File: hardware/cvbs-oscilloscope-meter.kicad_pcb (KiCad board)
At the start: 2 copper layers, 49.5 x 99.7 mm, 40 parts, among them J1 Conn_Coaxial_Power, J2 Conn_Coaxial_Power, J3 Conn_Coaxial_Power, J4 Conn_Coaxial_Power, Q1 2N3906, Q2 2N3906, Q3 2N3904, Q4 2N3904, Q5 2N3904, Q6 2N3904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

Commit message: Finished initial routing
Finished Routing - will need to check and revise
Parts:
- moved R15 22.6 mm to (115.4, 155.2), turned to 0 degrees
- moved C5 10.9 mm to (130.0, 155.2), turned to 90 degrees
- moved R14 8.81 mm to (125.6, 152.1), turned to 180 degrees
- moved U1 7.63 mm to (135.7, 145.7), turned to 90 degrees
- moved R13 7.62 mm to (115.4, 148.9), turned to 0 degrees
- moved Q6 2.57 mm to (131.3, 110.2), turned to 180 degrees
- moved U4 2.17 mm to (135.7, 156.5), turned to 90 degrees
- moved RV1 1.71 mm to (132.1, 171.6)
- moved RV2 1.71 mm to (127.9, 161.6)
- moved J4 1.62 mm to (130.0, 182.8)
- moved MK4 1.42 mm to (149.7, 187.6)
- moved MK3 1.42 mm to (110.3, 187.6)
- moved MK1 1.27 mm to (110.3, 111.2)
- moved MK2 1.27 mm to (149.7, 111.2)
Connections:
- U4 pad 1: (no net) -> Z
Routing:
- net +9V: track 0.00 -> 100.1 mm
- net Z: track 0.00 -> 67.2 mm
- net Y: track 0.00 -> 52.0 mm
- net Net-(D1-Pad2): track 0.00 -> 47.7 mm
- net COMP_VIDEO_IN: track 0.00 -> 47.2 mm
- net Net-(R13-Pad1): track 0.00 -> 43.5 mm
- net Net-(C5-Pad1): track 0.00 -> 29.9 mm
- net Net-(C2-Pad1): track 0.00 -> 28.9 mm
- net X: track 0.00 -> 27.4 mm
- net Net-(RV2-Pad2): track 0.00 -> 27.3 mm
- net Net-(Q3-Pad2): track 0.00 -> 24.8 mm
- net Net-(Q4-Pad1): track 0.00 -> 22.5 mm
- net Net-(Q2-Pad2): track 0.00 -> 22.3 mm
- net Net-(Q5-Pad1): track 0.00 -> 19.4 mm
- net Net-(R13-Pad2): track 0.00 -> 19.2 mm
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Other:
- board size 49.5 x 99.7 mm -> 47 x 99.1 mm

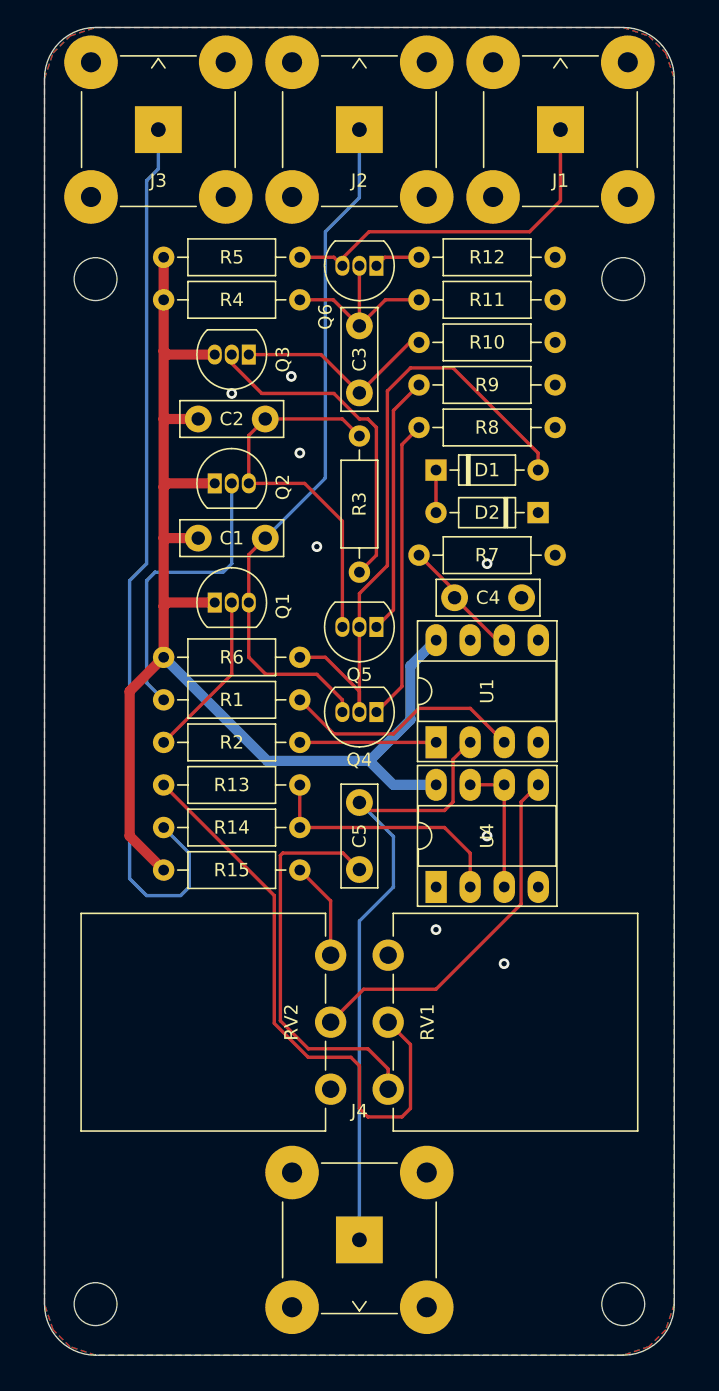
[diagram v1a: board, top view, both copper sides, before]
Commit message: New update
- Updated README
- Added power and LED circuitry
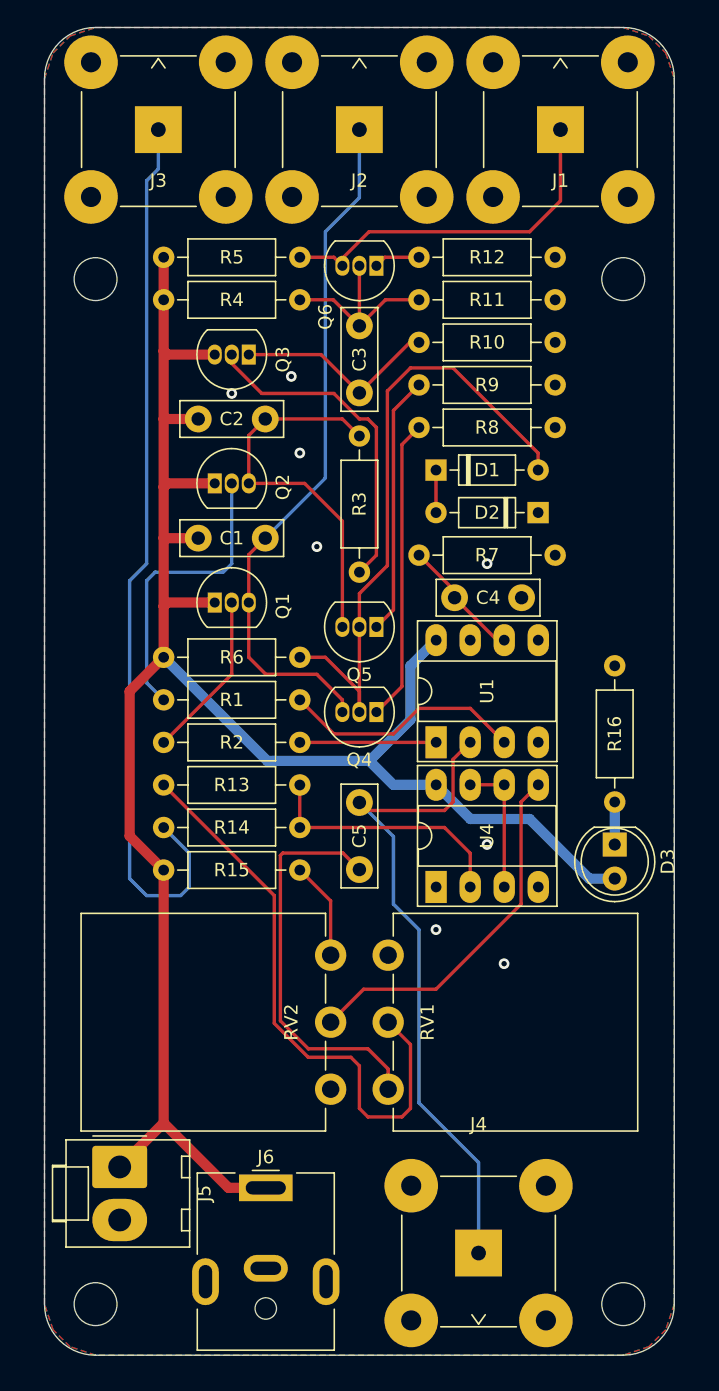
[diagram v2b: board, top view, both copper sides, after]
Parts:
- added D3: Indicator, LED_THT:LED_D5.0mm, F.Cu at (149.1, 153.3)
- added J5: Conn_01x02, Connector_Molex:Molex_KK-396_A-41791-0002_1x02_P3.96mm_Vertical, F.Cu at (112.1, 177.4)
- added J6: Conn_01x02, Connector_BarrelJack:BarrelJack_CUI_PJ-063AH_Horizontal, F.Cu at (123.0, 179.0)
- added R16: 2.4k, Resistor_THT:R_Axial_DIN0207_L6.3mm_D2.5mm_P10.16mm_Horizontal, F.Cu at (149.1, 150.2)
- moved J4 8.94 mm to (138.9, 183.8)
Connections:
- U4 pad 1: Z -> (no net)
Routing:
- net +9V: track 100.1 -> 149.5 mm
- net Net-(D3-Pad1): track 0.00 -> 3.18 mm
- net COMP_VIDEO_IN: track 47.2 -> 49.8 mm
